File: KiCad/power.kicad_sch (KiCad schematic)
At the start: 42 parts, among them J1 Conn_01x02_Pin, J2 Conn_01x02_Pin, Q1 AO3401A, Q2 AO3401A, Q3 AO3401A, U1 Battery Charger, U2 LMV321, U4 XC6206PxxxMR, u3 battery holder

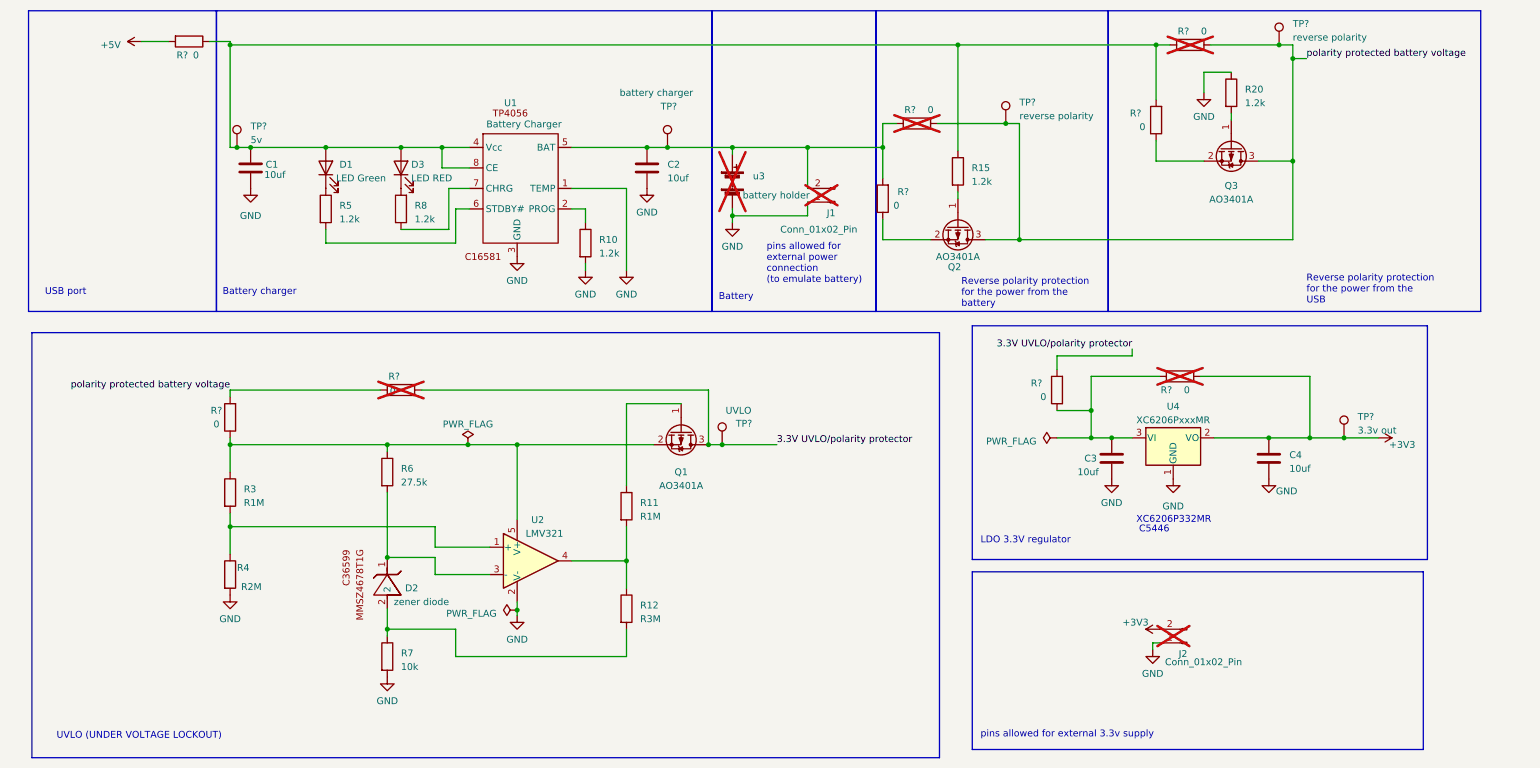
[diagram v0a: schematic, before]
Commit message: Removed extra 0ohms, added microcontroller male header
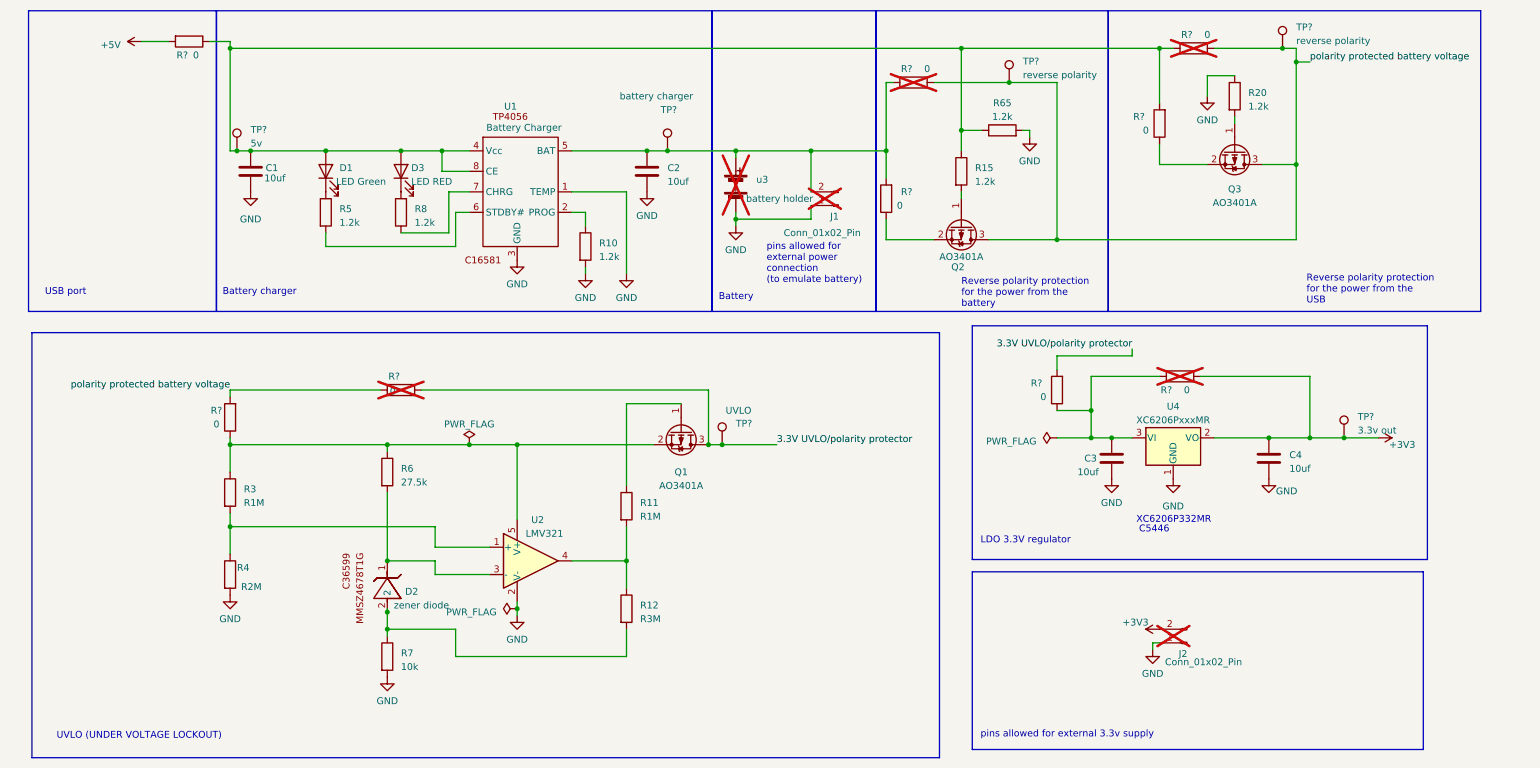
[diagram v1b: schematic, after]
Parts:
- added R65: 1.2k, footprint:R0805, symbol Device:R
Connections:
- net GND: now also R65.2
- net at C1.1, D1.2 (A), D3.2 (A)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: now also R65.1
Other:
- moved on the sheet: C1, C2, D1, D2, D3, J1, Q2, Q3, R10, R15, R20, R5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

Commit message: power cirucat chang
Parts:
- removed R15, R65: 1.2k, footprint:R0805, symbol Device:R
- added R12: R3M, footprint:R0603, symbol Device:R
- added R8: 1.2k, footprint:R0805, symbol Device:R
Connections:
- net +5V: now also R8.1
- net GND: now also R20.2, R12.1; no longer R20.1
- net polarity protected battery voltage: now also Q2.2 (S), Q3.2 (S); no longer Q2.3 (D), Q3.3 (D)
- net at Q2.1 (G): now also R12.2, R8.2
- net at Q3.1 (G): now also R20.1; no longer R20.2
- net at R?.1: now also Q3.3 (D); no longer Q3.2 (S)
- net at R?.1: now also Q2.3 (D); no longer Q2.2 (S)
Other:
- moved on the sheet: Q2, Q3, R20, R?

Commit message: Significant schematic changes
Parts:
- removed R12: R3M, footprint:R0603, symbol Device:R
- removed R?: 0, footprint:R0603, symbol Device:R
- added Q1: AO3401A, footprint:SOT-23_L2.9-W1.3-P1.90-LS2.4-BR, symbol Transistor_FET:AO3401A
- added R1: 1M, footprint:R0603, symbol Device:R
- added R4: 1.2k, footprint:R0805, symbol Device:R
- added R? (x3): 0, footprint:R0603, symbol Device:R
- renumbered D2 to D1, D1 to D2, Q1 to Q2, Q2 to Q3, Q3 to Q4, R5 to R10, R8 to R12, R11 to R13, R12 to R14, R10 to R15, R8 to R18, R20 to R23, R3 to R6, R4 to R7, R6 to R8, R7 to R9, U2 to U1, U1 to U2
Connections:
- net +3V3: now also R?.1; no longer C4.1, R?.1, TP?.1, U4.2 (VO)
- net +5V: now also R1.1, R?.2, R?.2
- net 3.3V UVLO/polarity protector: now also R?.2
- net GND: now also R1.2, R4.2
- net at C1.1, D2.2 (A), D3.2 (A)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: now also Q1.2 (S), R?.1
- net at C3.1, R?.1, U4.3 (VI): no longer R?.2
- new net: C4.1, R?.1, R?.2, TP?.1, U4.2 (VO)
- new net: Q1.1 (G), R4.1
- new net: Q1.3 (D), R?.1
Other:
- note added: "+5V pulled down to GND when disconnected"
- note added: "5V in"
- note added: "5V reverse polarity protection"
- note added: "Battery reverse polarity protection and block battery when on 5V power"
- note added: "Prevents power from feeding back into 5V in when on battery power"
- note added: "pins allow for external power connection (to emulate battery)"
- note added: "pins allowed for external 3.3v supply (in case of total power system failure)"
- note added: "pulldown to GND when not connected"
- note removed: "Reverse polarity protection for the power from the USB"
- note removed: "Reverse polarity protection for the power from the battery"
- note removed: "USB port"
- note removed: "pins allowed for external 3.3v supply"
- note removed: "pins allowed for external power connection (to emulate battery)"
- moved on the sheet: C1, C2, C4, D2, D3, J1, Q3, Q4, R10, R12, R15, R18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

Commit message: any residual changes from previous commit
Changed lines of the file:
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@@
   (junction (at 125.73 128.27) (diameter 0) (color 0 0 0 0)
   )
+  (junction (at 81.28 140.97) (diameter 0) (color 0 0 0 0)
+  )
   (junction (at 140.97 106.68) (diameter 0) (color 0 0 0 0)
   )
@@
   (junction (at 105.41 137.16) (diameter 0) (color 0 0 0 0)
   )
-  (junction (at 81.28 140.97) (diameter 0) (color 0 0 0 0)
-  )
-  (junction (at 81.28 137.795) (diameter 0) (color 0 0 0 0)
-  )
   (junction (at 143.51 52.07) (diameter 0) (color 0 0 0 0)
   )
@@
   (junction (at 243.84 105.41) (diameter 0) (color 0 0 0 0)
   )
+  (junction (at 267.97 105.41) (diameter 0) (color 0 0 0 0)
+  )
   (junction (at 105.41 52.07) (diameter 0) (color 0 0 0 0)
   )
@@
     (stroke (width 0) (type default))
   )
+  (wire (pts (xy 90.17 130.81) (xy 90.17 128.27))
+    (stroke (width 0) (type default))
+  )
+  (wire (pts (xy 173.99 64.77) (xy 173.99 62.23))
+    (stroke (width 0) (type default))
+  )
+  (wire (pts (xy 97.79 67.31) (xy 106.68 67.31))
+    (stroke (width 0) (type default))
+  )
+  (wire (pts (xy 199.39 39.37) (xy 209.55 39.37))
+    (stroke (width 0) (type default))
+  )
+  (wire (pts (xy 90.17 125.73) (xy 100.33 125.73))
+    (stroke (width 0) (type default))
+  )
+  (wire (pts (xy 125.73 114.3) (xy 125.73 99.06))
+    (stroke (width 0) (type default))
+  )
+  (wire (pts (xy 140.97 106.68) (xy 143.51 106.68))
+    (stroke (width 0) (type default))
+  )
+  (wire (pts (xy 237.49 105.41) (xy 243.84 105.41))
+    (stroke (width 0) (type default))
+  )
+  (wire (pts (xy 52.07 119.38) (xy 52.07 121.92))
+    (stroke (width 0) (type default))
+  )
+  (wire (pts (xy 160.02 52.07) (xy 173.99 52.07))
+    (stroke (width 0) (type default))
+  )
+  (wire (pts (xy 129.54 59.69) (xy 139.7 59.69))
+    (stroke (width 0) (type default))
+  )
+  (wire (pts (xy 52.07 121.92) (xy 52.07 127))
+    (stroke (width 0) (type default))
+  )
+  (wire (pts (xy 125.73 121.92) (xy 125.73 128.27))
+    (stroke (width 0) (type default))
+  )
+  (wire (pts (xy 125.73 140.97) (xy 125.73 146.05))
+    (stroke (width 0) (type default))
+  )
+  (wire (pts (xy 74.93 52.07) (xy 83.82 52.07))
+    (stroke (width 0) (type default))
+  )
+  (wire (pts (xy 69.85 52.07) (xy 74.93 52.07))
+    (stroke (width 0) (type default))
+  )
+  (wire (pts (xy 205.74 104.14) (xy 205.74 105.41))
+    (stroke (width 0) (type default))
+  )
+  (wire (pts (xy 52.07 97.79) (xy 52.07 96.52))
+    (stroke (width 0) (type default))
+  )
+  (wire (pts (xy 234.95 105.41) (xy 237.49 105.41))
+    (stroke (width 0) (type default))
+  )
+  (wire (pts (xy 96.52 106.68) (xy 105.41 106.68))
+    (stroke (width 0) (type default))
+  )
+  (wire (pts (xy 53.34 46.99) (xy 66.04 46.99))
+    (stroke (width 0) (type default))
+  )
+  (wire (pts (xy 219.71 90.17) (xy 219.71 88.9))
+    (stroke (width 0) (type default))
+  )
+  (wire (pts (xy 208.28 52.07) (xy 218.44 52.07))
+    (stroke (width 0) (type default))
+  )
+  (wire (pts (xy 147.32 52.07) (xy 160.02 52.07))
+    (stroke (width 0) (type default))
+  )
+  (wire (pts (xy 105.41 137.16) (xy 105.41 138.43))
+    (stroke (width 0) (type default))
+  )
+  (wire (pts (xy 125.73 146.05) (xy 93.98 146.05))
+    (stroke (width 0) (type default))
+  )
+  (wire (pts (xy 269.24 105.41) (xy 267.97 105.41))
+    (stroke (width 0) (type default))
+  )
+  (wire (pts (xy 267.97 105.41) (xy 265.43 105.41))
+    (stroke (width 0) (type default))
+  )
   (wire (pts (xy 81.28 137.795) (xy 81.28 140.97))
     (stroke (width 0) (type default))
   )
-  (wire (pts (xy 90.17 130.81) (xy 90.17 128.27))
-    (stroke (width 0) (type default))
-  )
-  (wire (pts (xy 173.99 64.77) (xy 173.99 62.23))
-    (stroke (width 0) (type default))
-  )
-  (wire (pts (xy 97.79 67.31) (xy 106.68 67.31))
-    (stroke (width 0) (type default))
-  )
-  (wire (pts (xy 199.39 39.37) (xy 209.55 39.37))
-    (stroke (width 0) (type default))
-  )
-  (wire (pts (xy 90.17 125.73) (xy 100.33 125.73))
-    (stroke (width 0) (type default))
-  )
-  (wire (pts (xy 125.73 114.3) (xy 125.73 99.06))
-    (stroke (width 0) (type default))
-  )
-  (wire (pts (xy 140.97 106.68) (xy 143.51 106.68))
-    (stroke (width 0) (type default))
-  )
-  (wire (pts (xy 237.49 105.41) (xy 243.84 105.41))
-    (stroke (width 0) (type default))
-  )
-  (wire (pts (xy 52.07 119.38) (xy 52.07 121.92))
-    (stroke (width 0) (type default))
-  )
-  (wire (pts (xy 160.02 52.07) (xy 173.99 52.07))
-    (stroke (width 0) (type default))
-  )
-  (wire (pts (xy 129.54 59.69) (xy 139.7 59.69))
-    (stroke (width 0) (type default))
-  )
-  (wire (pts (xy 52.07 121.92) (xy 52.07 127))
-    (stroke (width 0) (type default))
-  )
-  (wire (pts (xy 125.73 121.92) (xy 125.73 128.27))
-    (stroke (width 0) (type default))
-  )
-  (wire (pts (xy 125.73 140.97) (xy 125.73 146.05))
-    (stroke (width 0) (type default))
-  )
-  (wire (pts (xy 74.93 52.07) (xy 83.82 52.07))
-    (stroke (width 0) (type default))
-  )
-  (wire (pts (xy 69.85 52.07) (xy 74.93 52.07))
-    (stroke (width 0) (type default))
-  )
-  (wire (pts (xy 205.74 104.14) (xy 205.74 105.41))
-    (stroke (width 0) (type default))
-  )
-  (wire (pts (xy 52.07 97.79) (xy 52.07 96.52))
-    (stroke (width 0) (type default))
-  )
-  (wire (pts (xy 234.95 105.41) (xy 237.49 105.41))
-    (stroke (width 0) (type default))
-  )
-  (wire (pts (xy 96.52 106.68) (xy 105.41 106.68))
-    (stroke (width 0) (type default))
-  )
-  (wire (pts (xy 53.34 46.99) (xy 66.04 46.99))
-    (stroke (width 0) (type default))
-  )
-  (wire (pts (xy 219.71 90.17) (xy 219.71 88.9))
-    (stroke (width 0) (type default))
-  )
-  (wire (pts (xy 208.28 52.07) (xy 218.44 52.07))
-    (stroke (width 0) (type default))
-  )
-  (wire (pts (xy 147.32 52.07) (xy 160.02 52.07))
-    (stroke (width 0) (type default))
-  )
-  (wire (pts (xy 105.41 137.16) (xy 105.41 138.43))
-    (stroke (width 0) (type default))
-  )
-  (wire (pts (xy 125.73 146.05) (xy 93.98 146.05))
-    (stroke (width 0) (type default))
-  )
-  (wire (pts (xy 269.24 105.41) (xy 265.43 105.41))
-    (stroke (width 0) (type default))
-  )
   (wire (pts (xy 52.07 105.41) (xy 52.07 106.68))
     (stroke (width 0) (type default))
@@
   )
   (wire (pts (xy 81.28 106.68) (xy 96.52 106.68))
-    (stroke (width 0) (type default))
-  )
-  (wire (pts (xy 81.28 137.16) (xy 81.28 137.795))
     (stroke (width 0) (type default))
   )
@@
         )
       )
+    )
+  )
+  (symbol (lib_id "power:PWR_FLAG") (at 267.97 105.41 0) (unit 1)
+    (in_bom yes) (on_board yes) (dnp no)
+    (property "Reference" "#FLG07" (at 267.97 103.505 0)
+      (effects (font (size 1.27 1.27)) hide)
+    )
+    (property "Value" "PWR_FLAG" (at 262.89 100.33 0)
+      (effects (font (size 1.27 1.27)) (justify left))
+    )
+    (property "Footprint" "" (at 267.97 105.41 0)
+      (effects (font (size 1.27 1.27)) hide)
+    )
+    (property "Datasheet" "~" (at 267.97 105.41 0)
+      (effects (font (size 1.27 1.27)) hide)
+    )
+    (pin "1")
+    (instances
+      (project "EEE3088F_CKR"
+        (path "/31e5d740-f3fb-4029-be8d-dfdc4f653d72/d53a003e-af2e-46c6-8ee9-c5701cef8adb"
+          (reference "#FLG07") (unit 1)
+        )
+      )
+      (project "power"
+        (path "/d9c34bc1-cf5e-42ef-a2b2-2cfbae723006"
+          (reference "#FLG03") (unit 1)
+        )
+      )

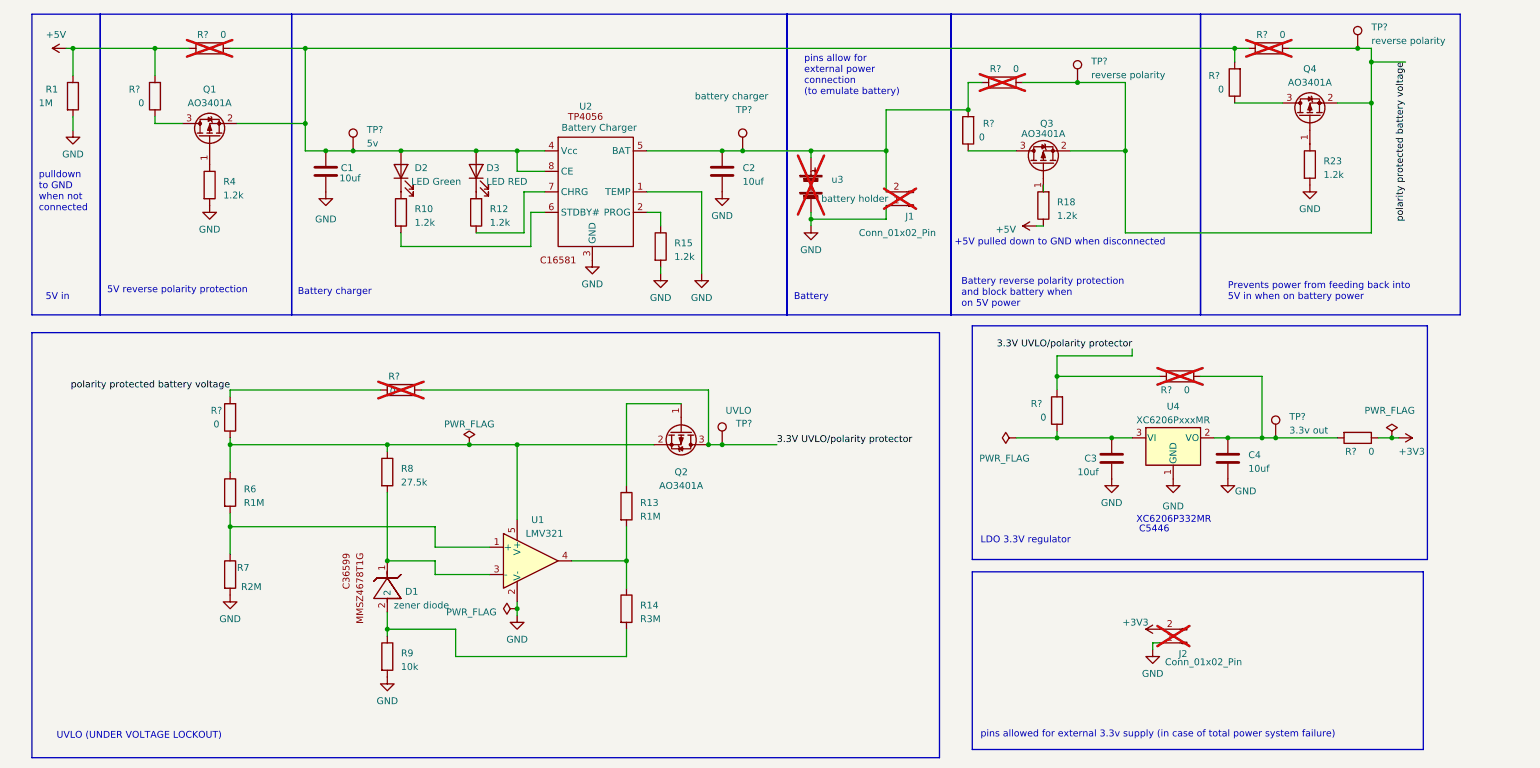
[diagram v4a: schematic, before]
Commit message: Corrected all part numbers and small schematic changes
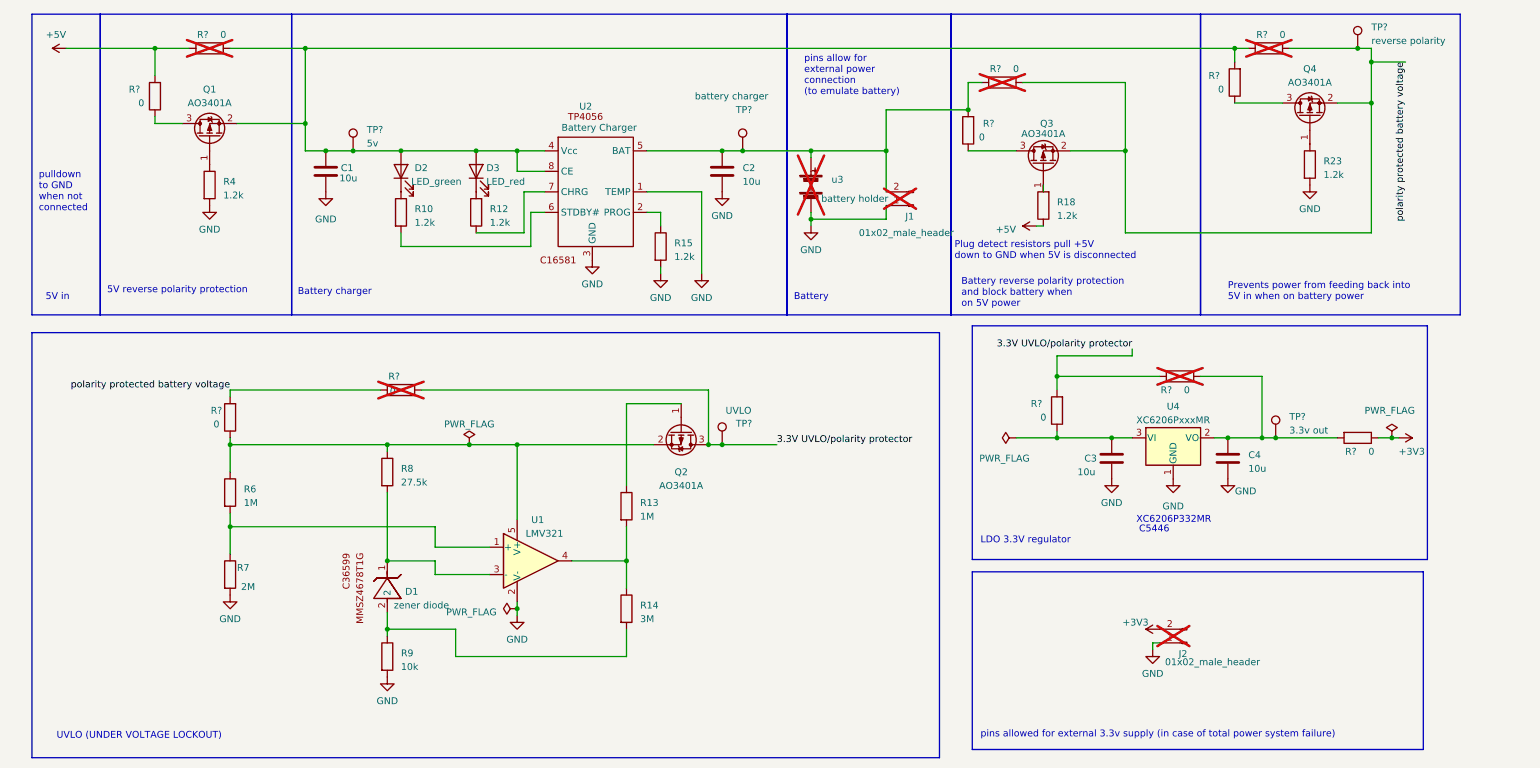
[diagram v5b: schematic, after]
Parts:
- removed R1: 1M, footprint:R0603, symbol Device:R
- removed TP?: reverse polarity, footprint:Testpoint_2.54mm, symbol Connector:TestPoint
- C1: value 10uf -> 10u; JLC code C2988620 -> C19702
- C2, C3, C4: value 10uf -> 10u
- D2: value LED Green -> LED_green; JLC code C2296 -> C72043; Part name 17-21SUYC/TR8 -> 19-217/GHC-YR1S2/3T; cost per unit 0,0119 -> 0.0264
- D3: value LED RED -> LED_red; Part name LED_0603 -> KT-0603R; cost per unit 0,0054 -> 0.0054
- J1, J2: value Conn_01x02_Pin -> 01x02_male_header; JLC code C5116481 -> (none); Part name 2.54-1*2 -> (none)
- Q1, Q2, Q3, Q4: cost per unit 0,0797 -> 0,07965
- R13, R6: value R1M -> 1M
- R14: value R3M -> 3M
- R7: value R2M -> 2M
- R8: cost per unit 0,0018 -> 0,0017
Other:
- note added: "Plug detect resistors pull +5V down to GND when 5V is disconnected"
- note removed: "+5V pulled down to GND when disconnected"

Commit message: small changes
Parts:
- D2: footprint footprint:LED0805-R-RD -> (none)
- D3: footprint footprint:LED0603-RD -> (none)
- U1: value LMV321 -> LMV321IDBVR; cost per unit 0,1439 -> 0.1456
- U2: cost per unit 0,2064 -> 0.2148
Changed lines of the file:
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@@
       (effects (font (size 1.27 1.27)) (justify right))
     )
-    (property "Footprint" "footprint:LED0603-RD" (at 97.79 55.88 0)
+    (property "Footprint" "" (at 97.79 55.88 0)
       (effects (font (size 1.27 1.27)) hide)
     )
@@
       (effects (font (size 1.27 1.27)) (justify right))
     )
-    (property "Footprint" "footprint:LED0805-R-RD" (at 83.82 55.88 0)
+    (property "Footprint" "" (at 83.82 55.88 0)
       (effects (font (size 1.27 1.27)) hide)
     )
@@
       (effects (font (size 1.27 1.27)))
     )
-    (property "Value" "LMV321" (at 110.49 123.19 0)
+    (property "Value" "LMV321IDBVR" (at 110.49 123.19 0)
       (effects (font (size 1.27 1.27)))
     )
@@
       (effects (font (size 1.27 1.27)) hide)
     )
-    (property "cost per unit" "0,1439" (at 107.95 128.27 0)
+    (property "cost per unit" "0.1456" (at 107.95 128.27 0)
       (effects (font (size 1.27 1.27)) hide)
     )
@@
       (effects (font (size 1.27 1.27)) hide)
     )
-    (property "cost per unit" "0,2064" (at 119.38 57.15 0)
-      (effects (font (size 1.27 1.27)) hide)
-    )
+    (property "cost per unit" "0.2148" (at 119.38 57.15 0)
+      (effects (font (size 1.27 1.27)) hide)
+    )
